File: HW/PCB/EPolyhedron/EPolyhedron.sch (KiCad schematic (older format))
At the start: 62 parts, among them J1 piezoelectric element', J2 ISP, J3 Battery, U1 ATtiny24A-SSU, U2 CD74HC4511M, U3 CD74HC4511M, U4 LP3985

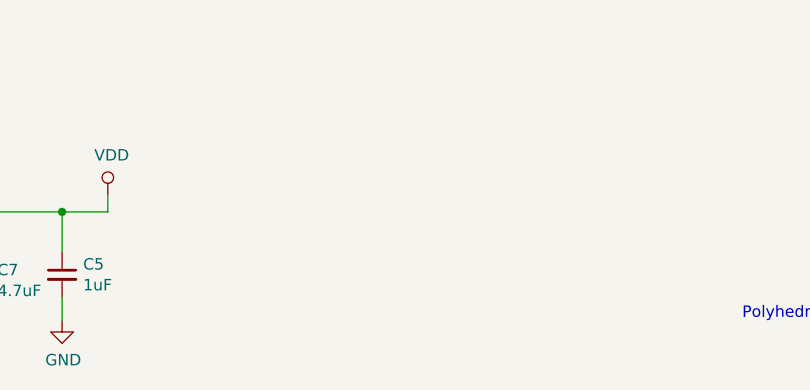
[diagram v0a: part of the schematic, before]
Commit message: Added d20 logo to silkscreen
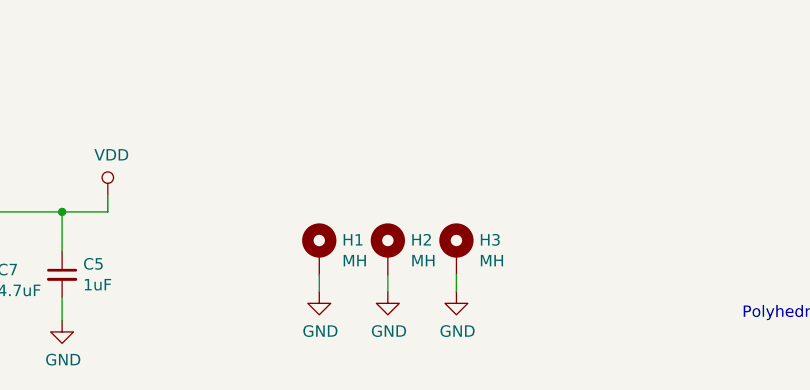
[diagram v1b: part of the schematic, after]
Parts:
- added H1, H2, H3: MH, MountingHole:MountingHole_2.2mm_M2_Pad, symbol Mechanical:MountingHole_Pad
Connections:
- net GND: now also H1.1, H2.1, H3.1
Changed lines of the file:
@@
 	1975 5625 1975 5500
 $Comp
-L power:VDD #PWR?
+L power:VDD #PWR0105
 U 1 1 5C8B3803
 P 3375 2100
-F 0 "#PWR?" H 3375 1950 50  0001 C CNN
+F 0 "#PWR0105" H 3375 1950 50  0001 C CNN
 F 1 "VDD" H 3392 2273 50  0000 C CNN
 F 2 "" H 3375 2100 50  0001 C CNN
@@
 $EndComp
 $Comp
-L power:VDD #PWR?
+L power:VDD #PWR0136
 U 1 1 5C8B388C
 P 1975 1025
-F 0 "#PWR?" H 1975 875 50  0001 C CNN
+F 0 "#PWR0136" H 1975 875 50  0001 C CNN
 F 1 "VDD" H 1992 1198 50  0000 C CNN
 F 2 "" H 1975 1025 50  0001 C CNN
@@
 $EndComp
 $Comp
-L power:VDD #PWR?
+L power:VDD #PWR0137
 U 1 1 5C8B3915
 P 1175 775
-F 0 "#PWR?" H 1175 625 50  0001 C CNN
+F 0 "#PWR0137" H 1175 625 50  0001 C CNN
 F 1 "VDD" H 1192 948 50  0000 C CNN
 F 2 "" H 1175 775 50  0001 C CNN
@@
 	3375 2625 3625 2625
 Connection ~ 3375 2625
+Wire Wire Line
+	5500 7300 5500 7375
+Wire Wire Line
+	5800 7300 5800 7375
+Wire Wire Line
+	6100 7300 6100 7375
+$Comp
+L power:GND #PWR03
+U 1 1 5CA18EA3
+P 6100 7375
+F 0 "#PWR03" H 6100 7125 50  0001 C CNN
+F 1 "GND" H 6105 7202 50  0000 C CNN
+F 2 "" H 6100 7375 50  0001 C CNN
+F 3 "" H 6100 7375 50  0001 C CNN
+	1    6100 7375
+	1    0    0    -1
+$EndComp
+$Comp
+L power:GND #PWR02
+U 1 1 5CA18E14
+P 5800 7375
+F 0 "#PWR02" H 5800 7125 50  0001 C CNN
+F 1 "GND" H 5805 7202 50  0000 C CNN
+F 2 "" H 5800 7375 50  0001 C CNN
+F 3 "" H 5800 7375 50  0001 C CNN
+	1    5800 7375
+	1    0    0    -1
+$EndComp
+$Comp
+L power:GND #PWR01
+U 1 1 5CA18D85
+P 5500 7375
+F 0 "#PWR01" H 5500 7125 50  0001 C CNN
+F 1 "GND" H 5505 7202 50  0000 C CNN
+F 2 "" H 5500 7375 50  0001 C CNN
+F 3 "" H 5500 7375 50  0001 C CNN
+	1    5500 7375
+	1    0    0    -1
+$EndComp
+$Comp
+L Mechanical:MountingHole_Pad H3
+U 1 1 5CA0C33F
+P 6100 7200
+F 0 "H3" H 6200 7251 50  0000 L CNN
+F 1 "MH" H 6200 7160 50  0000 L CNN
+F 2 "MountingHole:MountingHole_2.2mm_M2_Pad" H 6100 7200 50  0001 C CNN
+F 3 "~" H 6100 7200 50  0001 C CNN
+	1    6100 7200
+	1    0    0    -1
+$EndComp
+$Comp
+L Mechanical:MountingHole_Pad H2
+U 1 1 5CA0C288
+P 5800 7200
+F 0 "H2" H 5900 7251 50  0000 L CNN
+F 1 "MH" H 5900 7160 50  0000 L CNN
+F 2 "MountingHole:MountingHole_2.2mm_M2_Pad" H 5800 7200 50  0001 C CNN
+F 3 "~" H 5800 7200 50  0001 C CNN
+	1    5800 7200
+	1    0    0    -1
+$EndComp
+$Comp
+L Mechanical:MountingHole_Pad H1
+U 1 1 5CA0BCF3
+P 5500 7200
+F 0 "H1" H 5600 7251 50  0000 L CNN
+F 1 "MH" H 5600 7160 50  0000 L CNN
+F 2 "MountingHole:MountingHole_2.2mm_M2_Pad" H 5500 7200 50  0001 C CNN
+F 3 "~" H 5500 7200 50  0001 C CNN
+	1    5500 7200
+	1    0    0    -1
+$EndComp
 $EndSCHEMATC
